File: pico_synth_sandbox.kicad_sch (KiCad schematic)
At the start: 43 parts, among them J1 UART0, J2 LINEOUT, Q1 NMOS, SW1 RotaryEncoder_Switch, SW2 RESET, U1 Pico

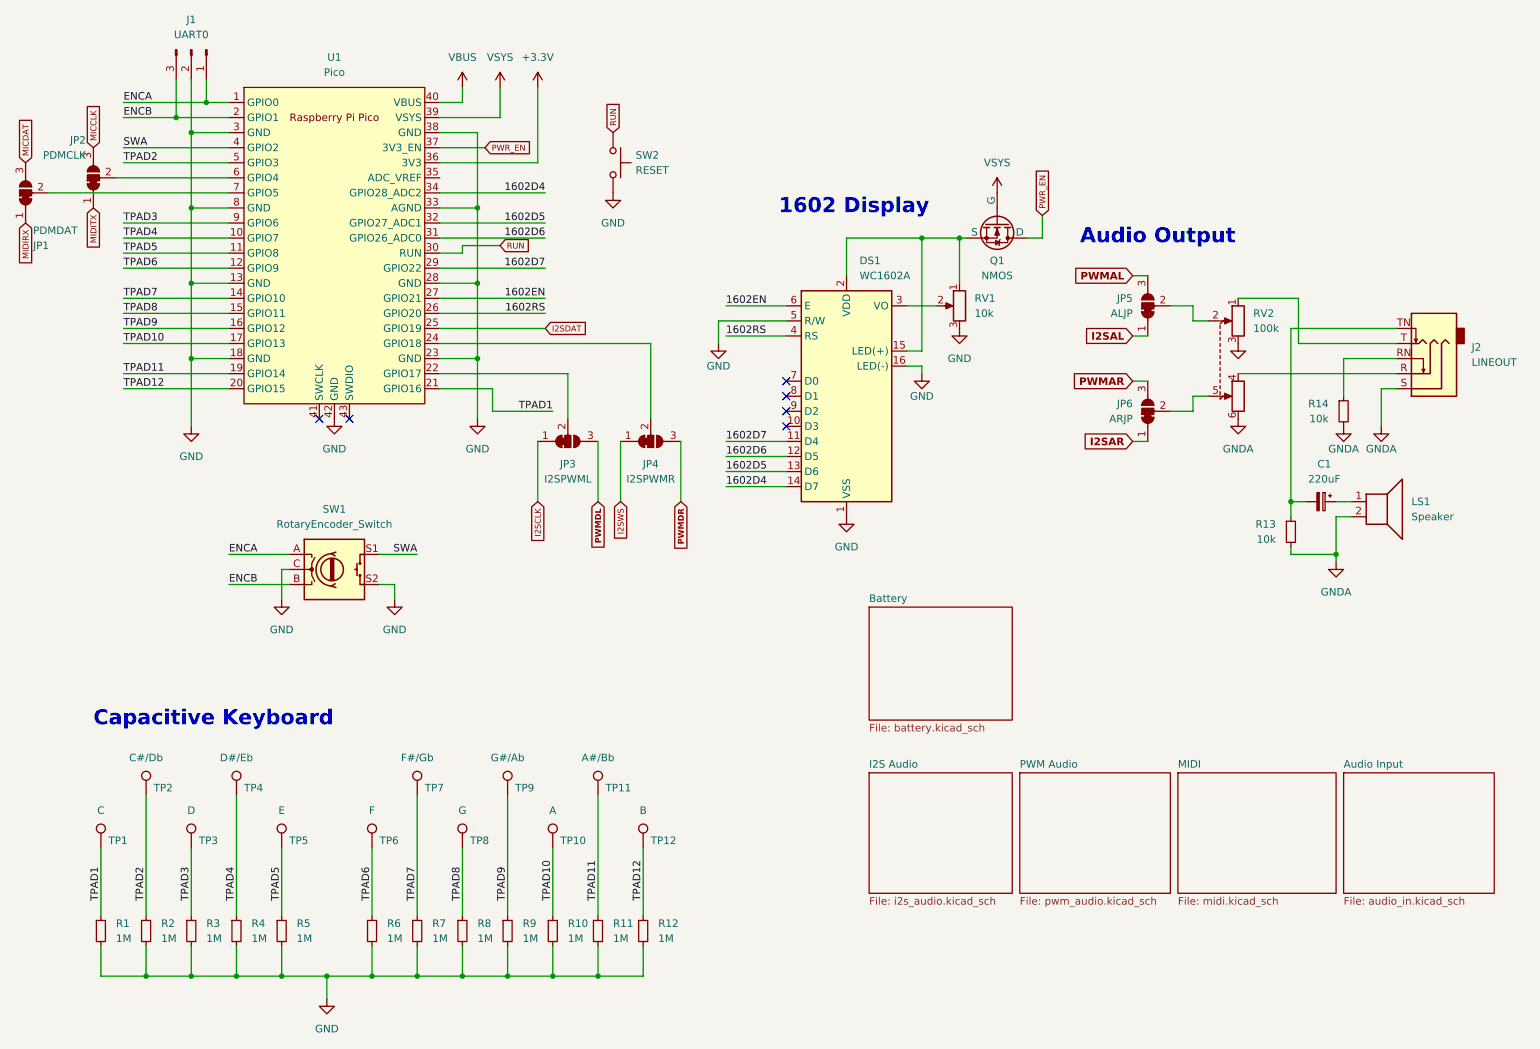
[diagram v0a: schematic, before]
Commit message: Updated to 5v power delivery.
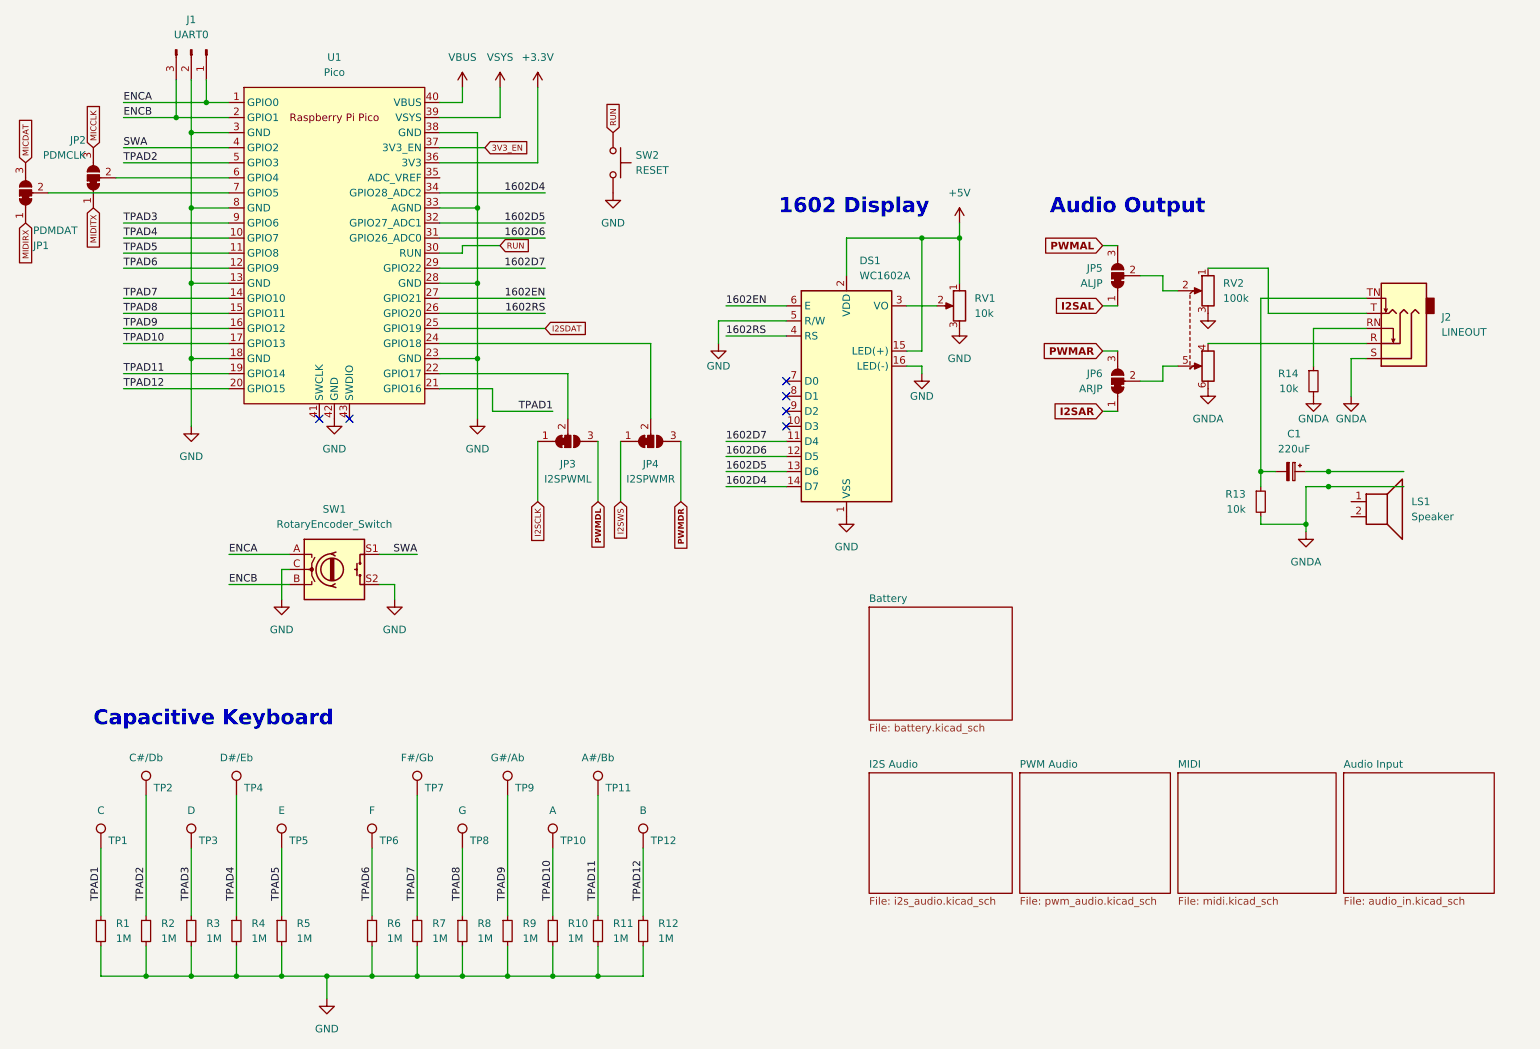
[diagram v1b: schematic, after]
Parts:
- removed Q1: NMOS, Package_TO_SOT_SMD:SOT-323_SC-70_Handsoldering, symbol Simulation_SPICE:NMOS
- C1: footprint Capacitor_THT:CP_Radial_D10.0mm_P5.00mm -> Capacitor_THT:CP_Radial_D5.0mm_P2.00mm
- R13, R14: footprint Resistor_THT:R_Axial_DIN0204_L3.6mm_D1.6mm_P5.08mm_Horizontal -> Resistor_THT:R_Axial_DIN0207_L6.3mm_D2.5mm_P7.62mm_Horizontal
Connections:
- net GNDA: no longer LS1.2
- net +5V: now reaches DS1.15 (LED(+)), DS1.2 (VDD), RV1.1
- net at LS1.1: no longer C1.1
- net PWR_EN renamed 3V3_EN
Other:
- moved on the sheet: C1, J2, JP5, JP6, R13, R14, RV2

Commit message: Added test points to speaker output.
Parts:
- added TP13, TP14: TestPoint, TestPoint:TestPoint_Pad_D2.0mm, symbol Connector:TestPoint
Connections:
- net GNDA: now also LS1.2, TP14.1
- net at LS1.1: now also C1.1, TP13.1
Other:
- moved on the sheet: LS1
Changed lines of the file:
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@@
     )
   )
-  (symbol (lib_id "Device:Speaker") (at 246.38 101.6 0) (unit 1)
-    (in_bom yes) (on_board yes) (dnp no) (fields_autoplaced)
-    (property "Reference" "LS1" (at 251.46 101.6 0)
-      (effects (font (size 1.27 1.27)) (justify left))
-    )
-    (property "Value" "Speaker" (at 251.46 104.14 0)
-      (effects (font (size 1.27 1.27)) (justify left))
-    )
-    (property "Footprint" "Connector_JST:JST_GH_SM02B-GHS-TB_1x02-1MP_P1.25mm_Horizontal" (at 246.38 106.68 0)
-      (effects (font (size 1.27 1.27)) hide)
-    )
-    (property "Datasheet" "~" (at 246.126 102.87 0)
+  (symbol (lib_id "Connector:TestPoint") (at 237.49 99.06 0) (mirror x) (unit 1)
+    (in_bom yes) (on_board yes) (dnp no)
+    (property "Reference" "TP14" (at 240.03 103.632 0)
+      (effects (font (size 1.27 1.27)) (justify left))
+    )
+    (property "Value" "TestPoint" (at 240.03 101.092 0)
+      (effects (font (size 1.27 1.27)) (justify left))
+    )
+    (property "Footprint" "TestPoint:TestPoint_Pad_D2.0mm" (at 242.57 99.06 0)
+      (effects (font (size 1.27 1.27)) hide)
+    )
+    (property "Datasheet" "~" (at 242.57 99.06 0)
+      (effects (font (size 1.27 1.27)) hide)
+    )
+    (pin "1")
+    (instances
+      (project "pico_synth_sandbox"
+        (path "/bfc01388-33ce-4b1a-9d2f-82d750172e5a"
+          (reference "TP14") (unit 1)
+        )
+      )
+    )
+  )
+  (symbol (lib_id "Device:Speaker") (at 255.27 96.52 0) (unit 1)
+    (in_bom yes) (on_board yes) (dnp no) (fields_autoplaced)
+    (property "Reference" "LS1" (at 260.35 96.52 0)
+      (effects (font (size 1.27 1.27)) (justify left))
+    )
+    (property "Value" "Speaker" (at 260.35 99.06 0)
+      (effects (font (size 1.27 1.27)) (justify left))
+    )
+    (property "Footprint" "Connector_JST:JST_GH_SM02B-GHS-TB_1x02-1MP_P1.25mm_Horizontal" (at 255.27 101.6 0)
+      (effects (font (size 1.27 1.27)) hide)
+    )
+    (property "Datasheet" "~" (at 255.016 97.79 0)
       (effects (font (size 1.27 1.27)) hide)
     )
@@
         )
       )
+    )
+  )
+  (symbol (lib_id "Connector:TestPoint") (at 237.49 96.52 0) (unit 1)
+    (in_bom yes) (on_board yes) (dnp no) (fields_autoplaced)
+    (property "Reference" "TP13" (at 240.03 91.948 0)
+      (effects (font (size 1.27 1.27)) (justify left))
+    )
+    (property "Value" "TestPoint" (at 240.03 94.488 0)
+      (effects (font (size 1.27 1.27)) (justify left))
+    )
+    (property "Footprint" "TestPoint:TestPoint_Pad_D2.0mm" (at 242.57 96.52 0)
+      (effects (font (size 1.27 1.27)) hide)
+    )
+    (property "Datasheet" "~" (at 242.57 96.52 0)
+      (effects (font (size 1.27 1.27)) hide)
+    )
+    (pin "1")
+    (instances
+      (project "pico_synth_sandbox"
+        (path "/bfc01388-33ce-4b1a-9d2f-82d750172e5a"
+          (reference "TP13") (unit 1)
+        )
+      )

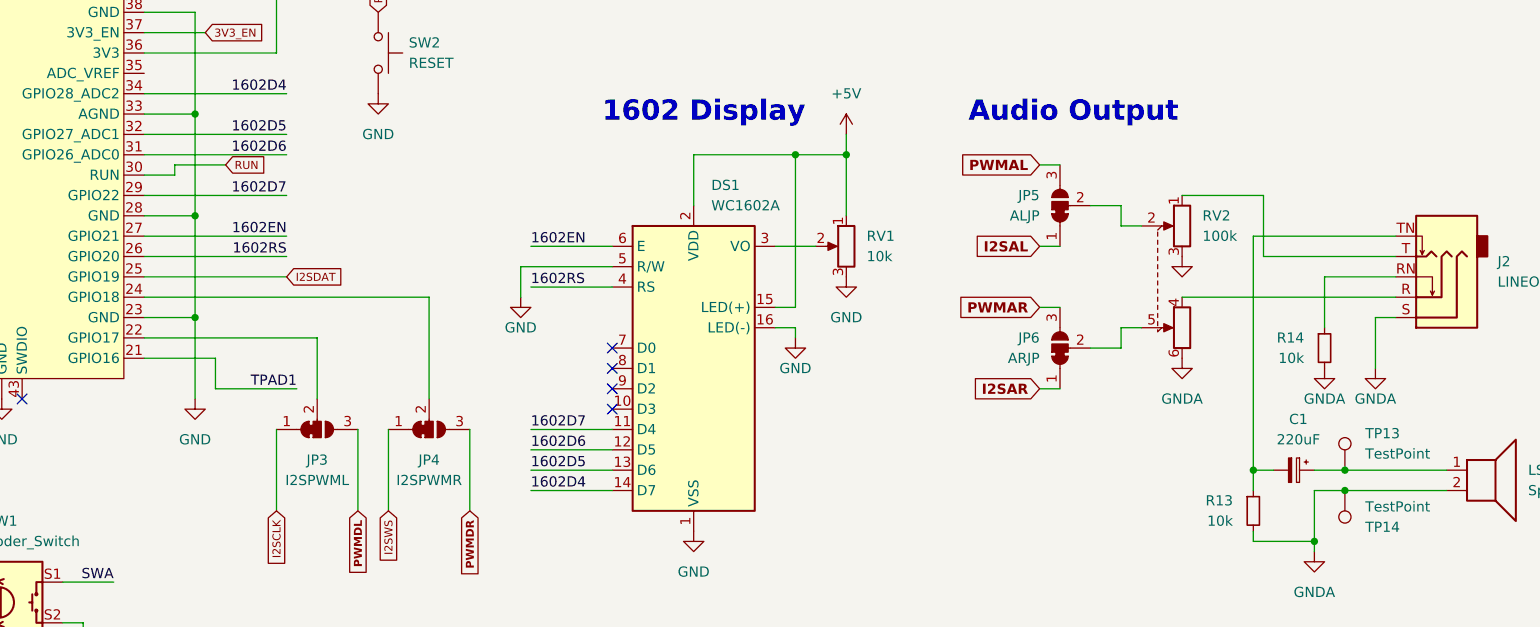
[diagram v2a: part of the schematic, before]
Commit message: Swap of TPAD1 with PWM/I2S pins to prevent issue with PWM slice allocation.
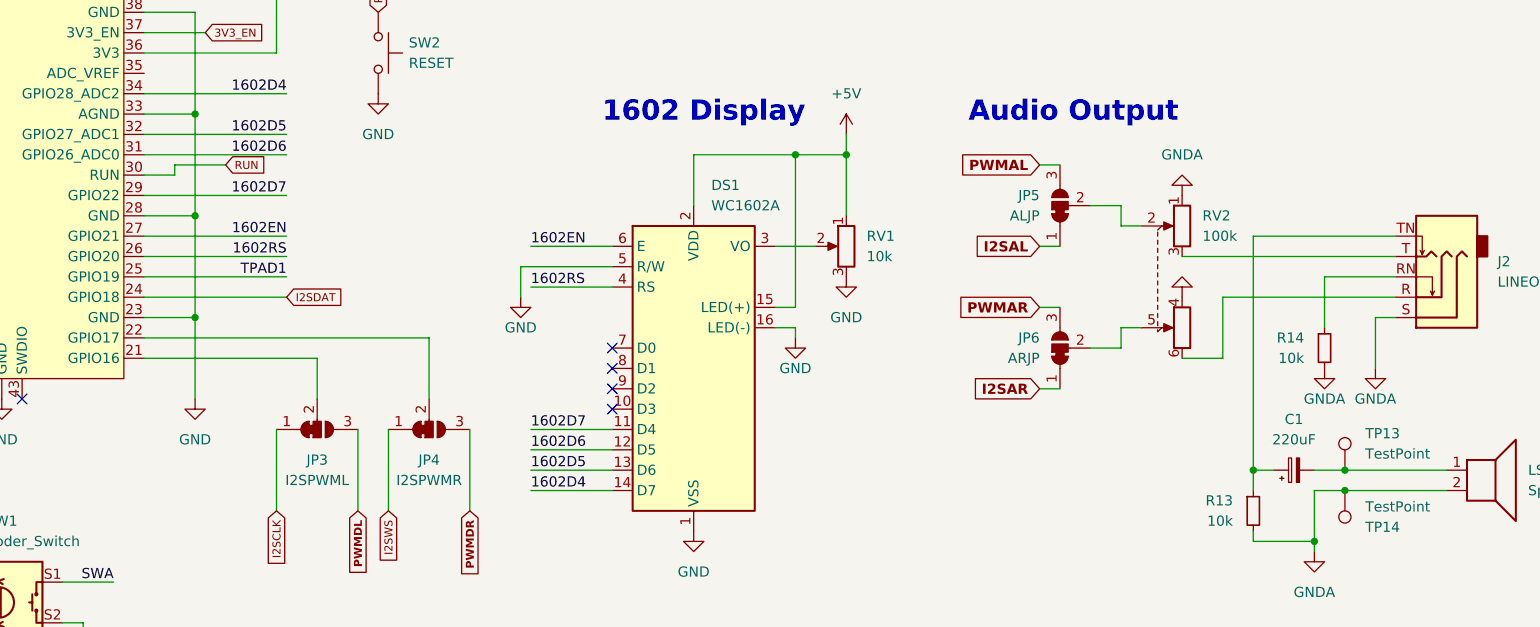
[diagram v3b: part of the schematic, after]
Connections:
- net GNDA: now also RV2.1, RV2.4; no longer RV2.3, RV2.6
- net I2SDAT: now also U1.24 (GPIO18); no longer U1.25 (GPIO19)
- net TPAD1: now also U1.25 (GPIO19); no longer U1.21 (GPIO16)
- net at J2.T: now also RV2.3; no longer RV2.1
- net at J2.R: now also RV2.6; no longer RV2.4
- net at J2.TN, R13.1: now also C1.1; no longer C1.2
- net at JP3.2 (C): now also U1.21 (GPIO16); no longer U1.22 (GPIO17)
- net at JP4.2 (C): now also U1.22 (GPIO17); no longer U1.24 (GPIO18)
- net at LS1.1, TP13.1: now also C1.2; no longer C1.1
